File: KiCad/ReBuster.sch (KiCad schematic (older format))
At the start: 11 parts, among them U3 SN74CBTD16210, U4 SN74LVC16T245DGVR, U5 SN74CBTD16210, U6 SN74CBTD16210, U7 74LVC2T45DC, U8 PLCC_84_plug, U9 PLCC_84_plug

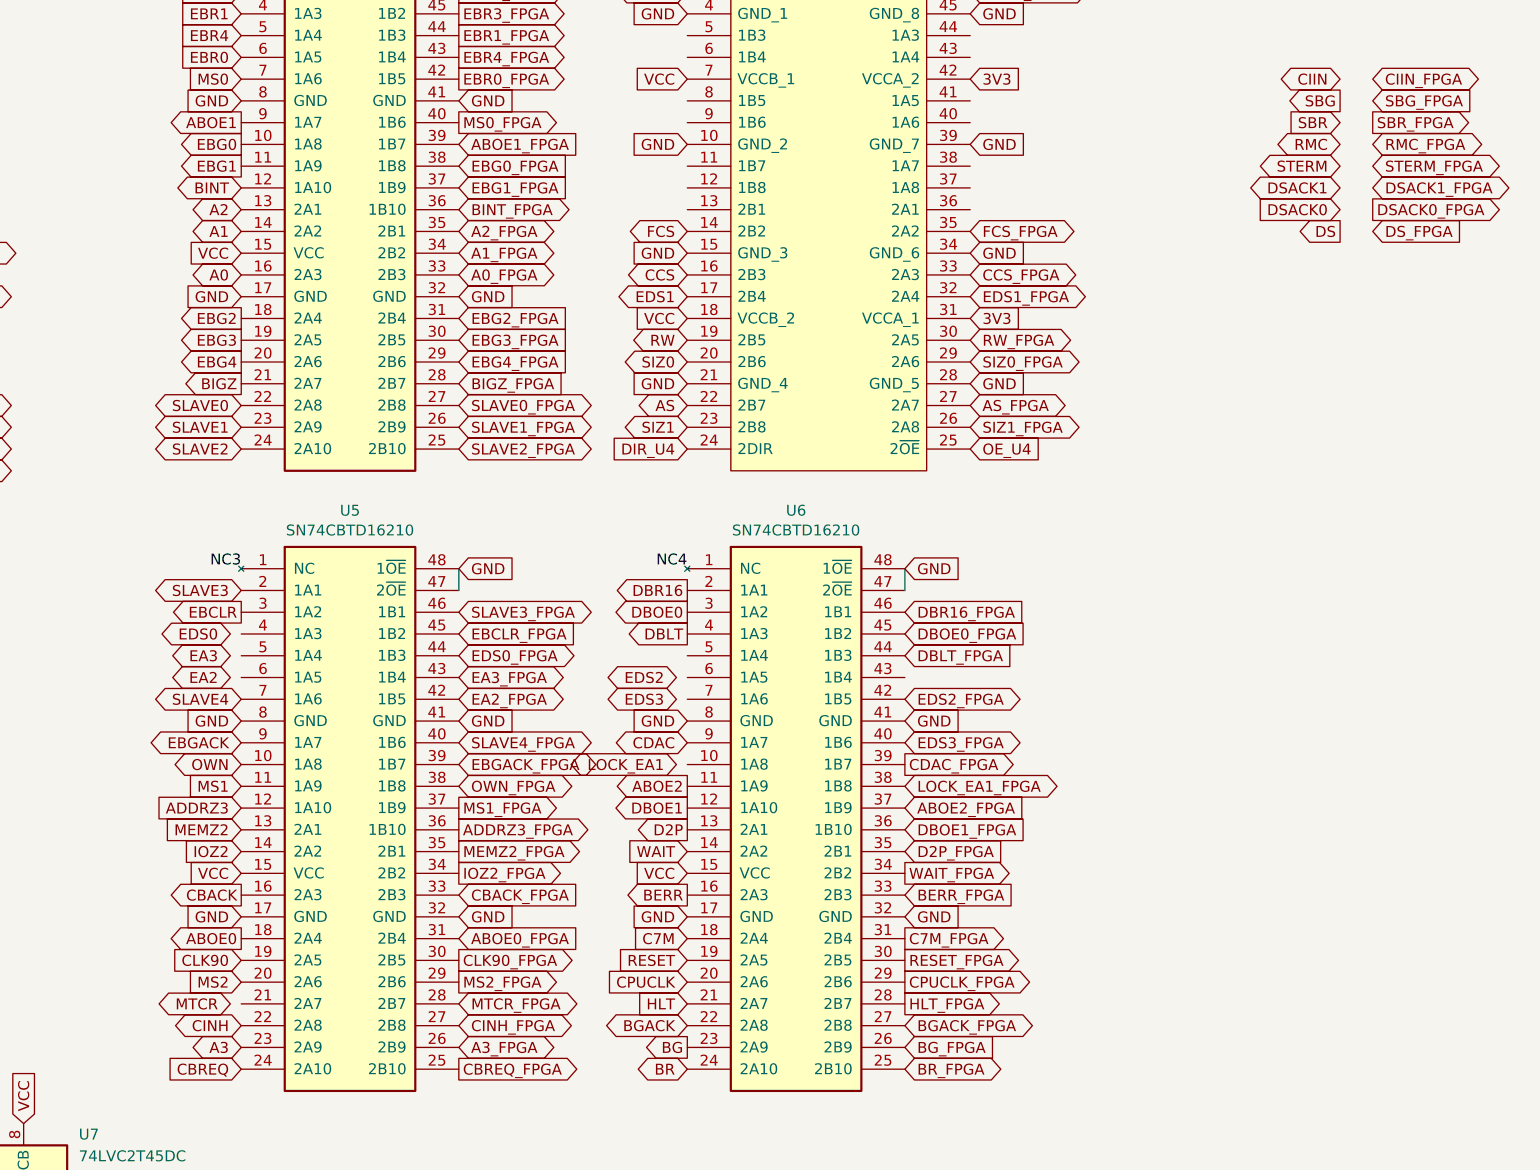
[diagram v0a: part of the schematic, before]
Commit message: Route STERM change N10 -> F12 in FPGA
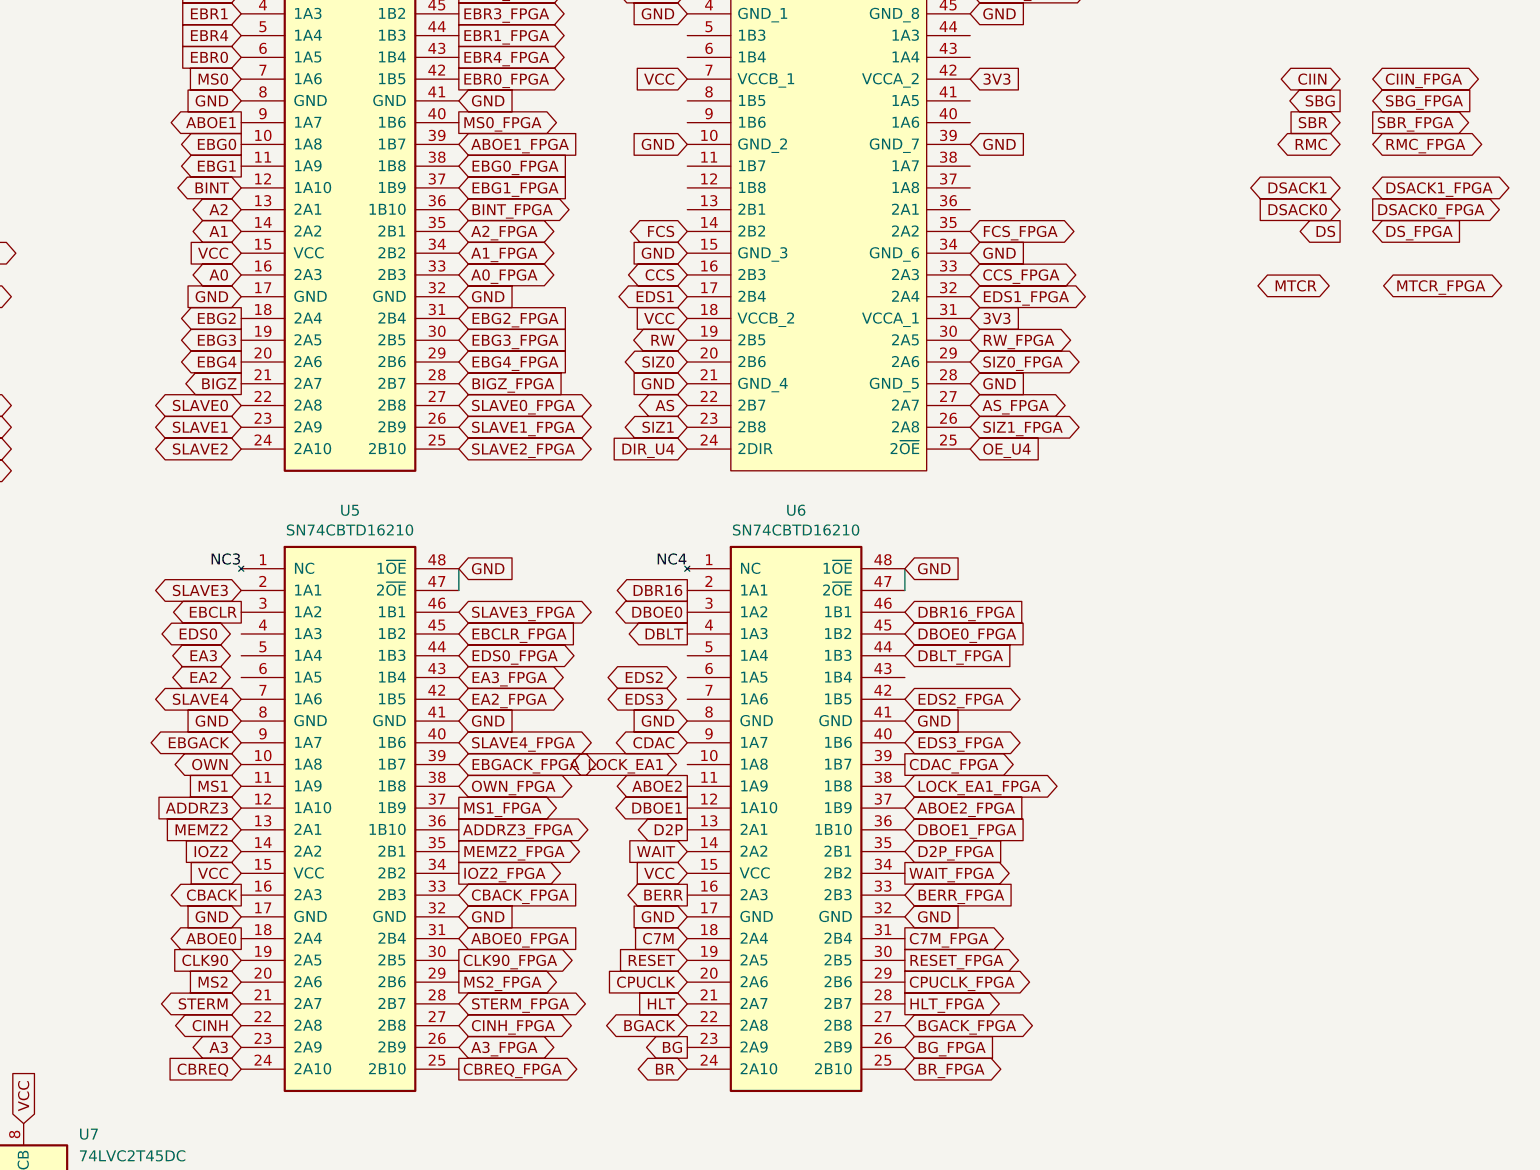
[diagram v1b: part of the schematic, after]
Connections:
- net MTCR_FPGA: no longer U5.28 (2B7)
- net STERM: now also U5.21 (2A7)
- net STERM_FPGA: now also U5.28 (2B7)
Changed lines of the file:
@@
 Text GLabel 10500 2850 2    50   BiDi ~ 0
 SIZ0_FPGA
-Text GLabel 12350 1950 2    50   BiDi ~ 0
+Text GLabel 8150 5800 2    50   BiDi ~ 0
 STERM_FPGA
 Text GLabel 12350 2250 2    50   Input ~ 0
@@
 Text GLabel 8150 5700 2    50   Output ~ 0
 MS2_FPGA
-Text GLabel 8150 5800 2    50   BiDi ~ 0
+Text GLabel 12400 2500 2    50   BiDi ~ 0
 MTCR_FPGA
 Text GLabel 8150 5900 2    50   BiDi ~ 0
@@
 Text GLabel 12200 2050 0    50   BiDi ~ 0
 DSACK1
-Text GLabel 12200 1950 0    50   BiDi ~ 0
+Text GLabel 7150 5800 0    50   BiDi ~ 0
 STERM
 Wire Wire Line
@@
 Text GLabel 7150 5700 0    50   Input ~ 0
 MS2
-Text GLabel 7100 5800 0    50   BiDi ~ 0
+Text GLabel 12150 2500 0    50   BiDi ~ 0
 MTCR
 Text GLabel 2750 4650 2    50   Output ~ 0

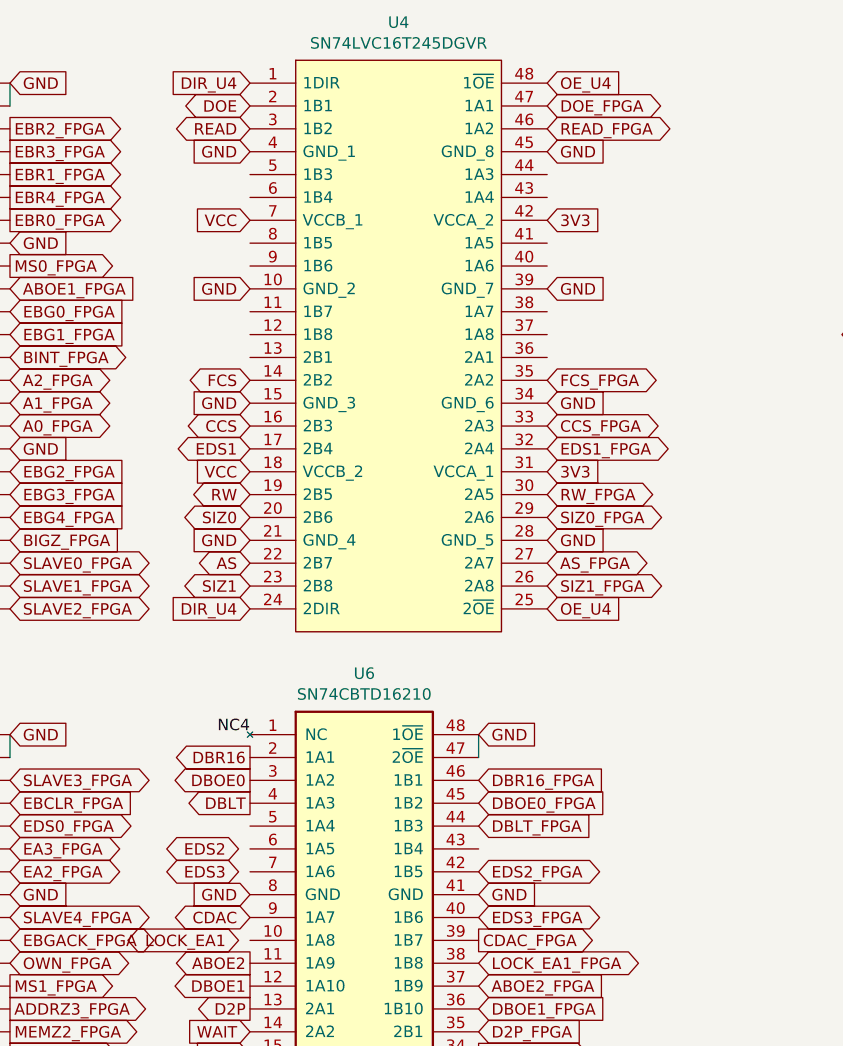
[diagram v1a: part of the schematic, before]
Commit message: Route EDS2 to U4 (SN74LVC16T245DGVR) change K13 -> K2 in FPGA
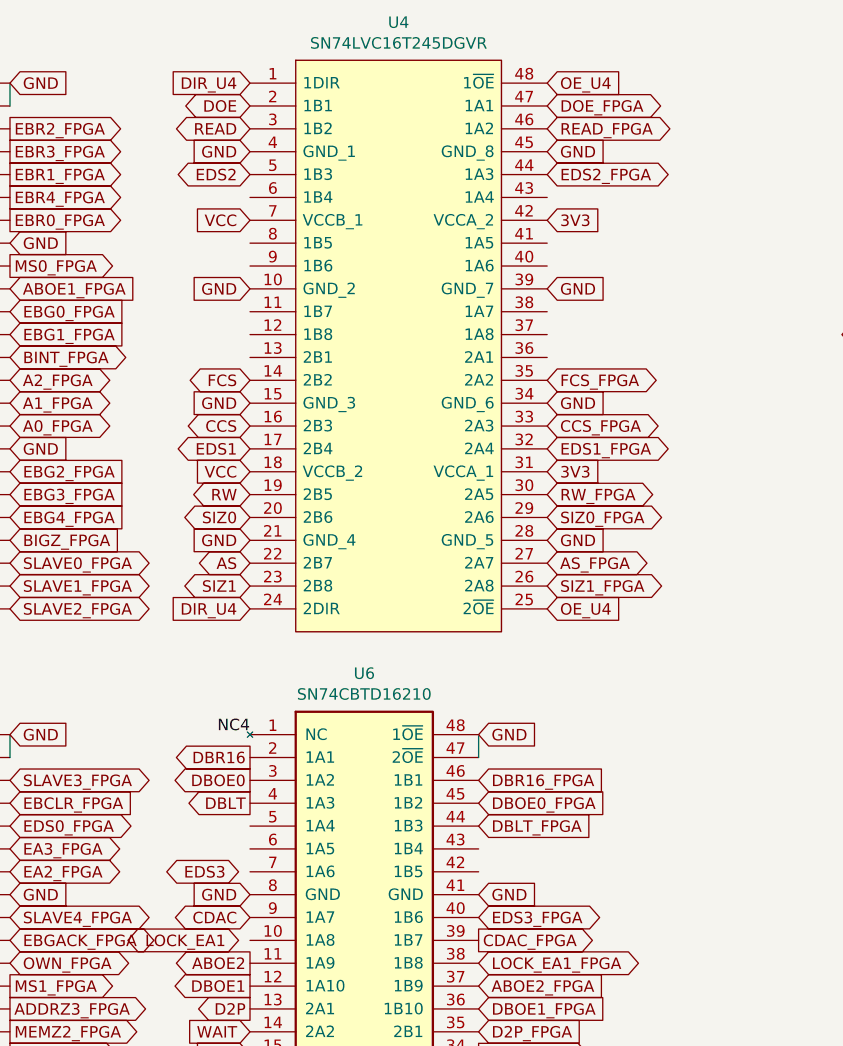
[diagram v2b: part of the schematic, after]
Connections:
- net EDS2: now also U4.5 (1B3)
- net EDS2_FPGA: now also U4.44 (1A3); no longer U6.42 (1B5)
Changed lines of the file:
@@
 Text GLabel 10500 1150 2    50   BiDi ~ 0
 READ_FPGA
-Text GLabel 10200 4400 2    50   BiDi ~ 0
+Text GLabel 10500 1350 2    50   BiDi ~ 0
 EDS2_FPGA
 Text GLabel 10200 4600 2    50   BiDi ~ 0
@@
 Text GLabel 9200 1150 0    50   BiDi ~ 0
 READ
-Text GLabel 9150 4300 0    50   BiDi ~ 0
+Text GLabel 9200 1350 0    50   BiDi ~ 0
 EDS2
 Text GLabel 9150 4400 0    50   BiDi ~ 0

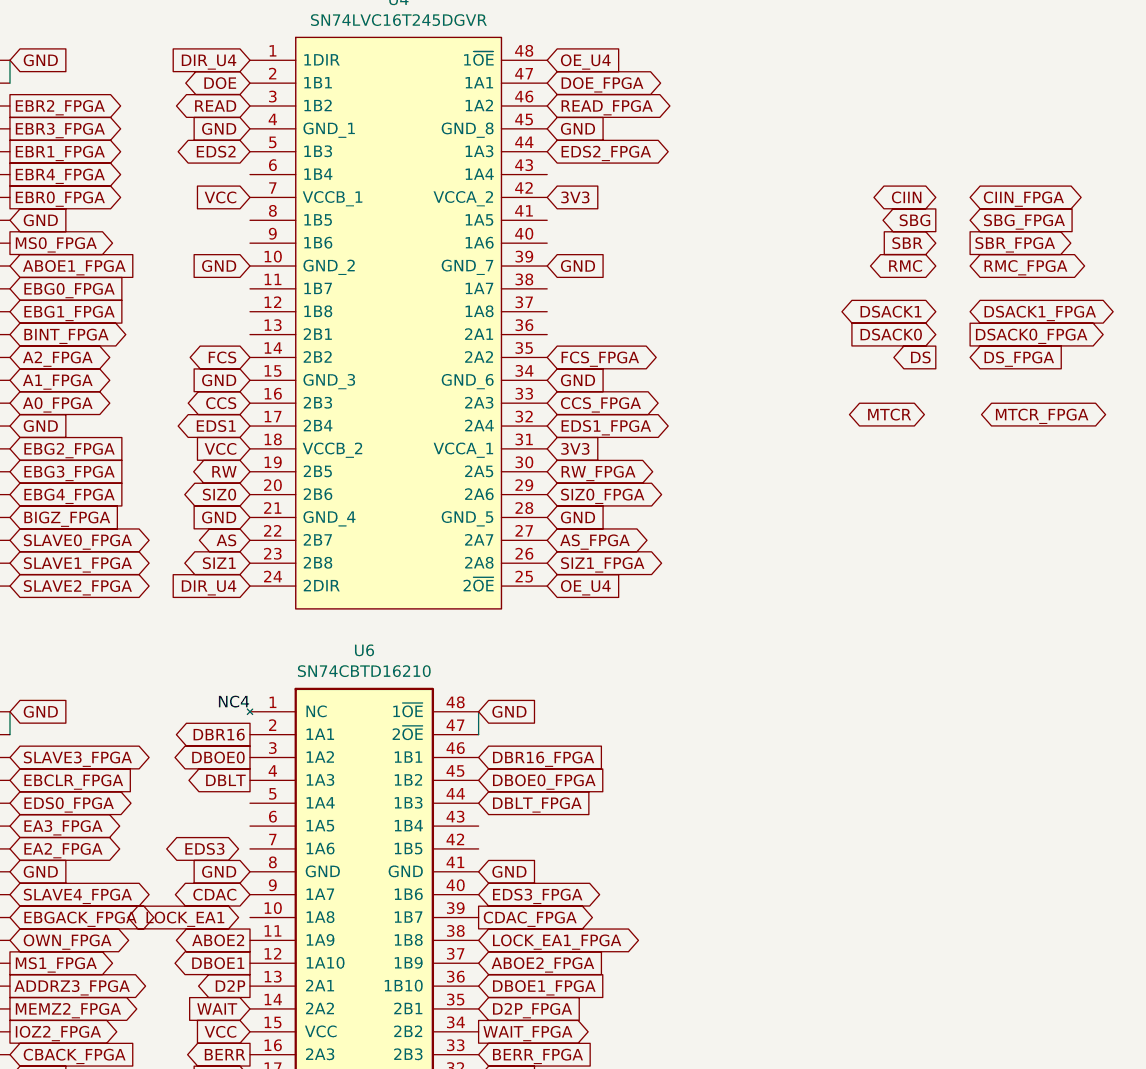
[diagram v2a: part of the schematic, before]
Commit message: Route EDS3 to U4 (SN74LVC16T245DGVR) change K12 -> M3 in FPGA
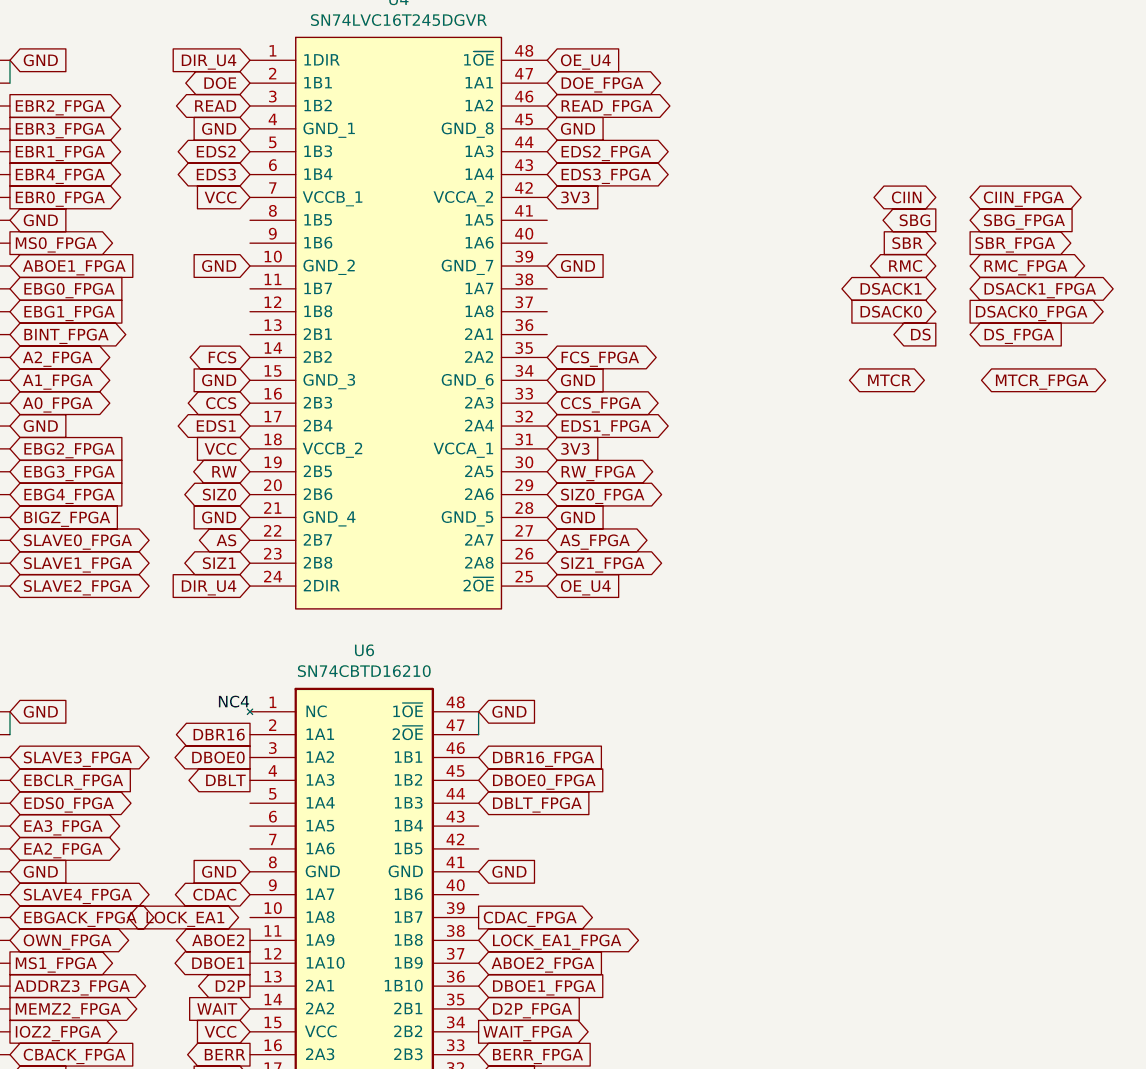
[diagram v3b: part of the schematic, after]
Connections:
- net EDS3: now also U4.6 (1B4)
- net EDS3_FPGA: now also U4.43 (1A4); no longer U6.40 (1B6)
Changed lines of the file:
@@
 Text GLabel 8150 5800 2    50   BiDi ~ 0
 STERM_FPGA
-Text GLabel 12350 2250 2    50   Input ~ 0
+Text GLabel 12350 2150 2    50   Input ~ 0
 DS_FPGA
 Text GLabel 10500 3050 2    50   BiDi ~ 0
@@
 Text GLabel 8150 5700 2    50   Output ~ 0
 MS2_FPGA
-Text GLabel 12400 2500 2    50   BiDi ~ 0
+Text GLabel 12400 2350 2    50   BiDi ~ 0
 MTCR_FPGA
 Text GLabel 8150 5900 2    50   BiDi ~ 0
@@
 Text GLabel 10500 1350 2    50   BiDi ~ 0
 EDS2_FPGA
-Text GLabel 10200 4600 2    50   BiDi ~ 0
+Text GLabel 10500 1450 2    50   BiDi ~ 0
 EDS3_FPGA
 Text GLabel 10200 4700 2    50   Output ~ 0
@@
 Text GLabel 9200 3050 0    50   BiDi ~ 0
 AS
-Text GLabel 12200 2250 0    50   Output ~ 0
+Text GLabel 12200 2150 0    50   Output ~ 0
 DS
-Text GLabel 12200 2150 0    50   Input ~ 0
+Text GLabel 12200 2050 0    50   Input ~ 0
 DSACK0
-Text GLabel 12200 2050 0    50   BiDi ~ 0
+Text GLabel 12200 1950 0    50   BiDi ~ 0
 DSACK1
 Text GLabel 7150 5800 0    50   BiDi ~ 0
@@
 Text GLabel 9200 1350 0    50   BiDi ~ 0
 EDS2
-Text GLabel 9150 4400 0    50   BiDi ~ 0
+Text GLabel 9200 1450 0    50   BiDi ~ 0
 EDS3
 Text GLabel 9150 4700 0    50   BiDi ~ 0
@@
 Text GLabel 7150 5700 0    50   Input ~ 0
 MS2
-Text GLabel 12150 2500 0    50   BiDi ~ 0
+Text GLabel 12150 2350 0    50   BiDi ~ 0
 MTCR
 Text GLabel 2750 4650 2    50   Output ~ 0
@@
 Text GLabel 8150 2450 2    50   BiDi ~ 0
 A0_FPGA
-Text GLabel 12350 2050 2    50   BiDi ~ 0
+Text GLabel 12350 1950 2    50   BiDi ~ 0
 DSACK1_FPGA
-Text GLabel 12350 2150 2    50   Output ~ 0
+Text GLabel 12350 2050 2    50   Output ~ 0
 DSACK0_FPGA
 $Comp
